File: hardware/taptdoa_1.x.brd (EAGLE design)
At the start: 64.8 x 63.2 mm, 67 parts, among them J1 105017-0001, U1 AP2112K-3.3TRG1, U2 STM32F103RBT6, Y1 8MHz

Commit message: v1.2 of board
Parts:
- removed TP21, TP22, TP4, TP5, TP6, TP7: TEST-POINT3X4, SparkFun-Connectors:PAD.03X.04
- moved J5 56.7 mm to (12.7, 58.4), turned to 0 degrees
- moved R6 46.6 mm to (15.2, 53.3)
- moved R1 46.2 mm to (53.3, 53.3)
- moved J3 44.0 mm to (35.6, 58.4), turned to 0 degrees
- moved R2 40.9 mm to (45.7, 53.3)
- moved R4 37.5 mm to (22.9, 53.3)
- moved R5 37.1 mm to (38.1, 53.3)
- moved R3 28.4 mm to (30.5, 53.3)
- moved TP3 21.0 mm to (36.1, 17.5)
- moved J2 19.4 mm to (16.5, 41.9), turned to 0 degrees
- moved TP2 17.0 mm to (35.9, 19.3)
- moved R15 16.5 mm to (55.6, 40.4)
- moved J1 15.2 mm to (63.2, 40.6)
- moved X1 7.73 mm to (5.08, 49.5)
- moved C1 6.84 mm to (15.2, 31.8)
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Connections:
- removed net PC0: R1.1, U2.8
- removed net PC1: R2.1, U2.9
- removed net PC2: R5.1, U2.10
- removed net PC3: R3.1, U2.11
- removed net PC4: R4.1, U2.24
- removed net PC5: R6.1, U2.25
- net OPAMP3_OUT: now also TP2.P$1; no longer TP21.P$1
- net PB2: now also TP3.P$1; no longer TP22.P$1
- net PB3: now also R1.1; no longer TP7.P$1
- net PB4: now also R2.1; no longer TP6.P$1
- net PB5: now also R5.1; no longer TP5.P$1
- net PB6: now also R3.1; no longer TP4.P$1
- net PB7: now also R4.1; no longer TP3.P$1
- net PB8: now also R6.1; no longer TP2.P$1
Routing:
- net +5V: track 60.5 -> 2.56 mm, vias 0 -> 1
- net PC3: track 32.6 -> 0.00 mm, vias 2 -> 0
- net PB8: track 2.27 -> 32.5 mm
- net PB3: track 4.86 -> 33.7 mm
- net PC4: track 28.6 -> 0.00 mm, vias 2 -> 0
- net PC5: track 27.9 -> 0.00 mm, vias 2 -> 0
- net PC0: track 27.7 -> 0.00 mm
- net PB4: track 2.13 -> 27.0 mm
- net PC1: track 23.0 -> 0.00 mm
- net PB7: track 4.89 -> 26.6 mm
- net PC2: track 21.0 -> 0.00 mm
- net PB6: track 3.42 -> 20.2 mm
- net USB_DP: track 40.4 -> 25.0 mm
- net PB5: track 6.32 -> 20.6 mm
- net NRST: track 34.3 -> 21.3 mm, vias 0 -> 2
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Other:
- board text added: "TapTDOA v1.2"
- board text removed: "TapTDOA v1.1"

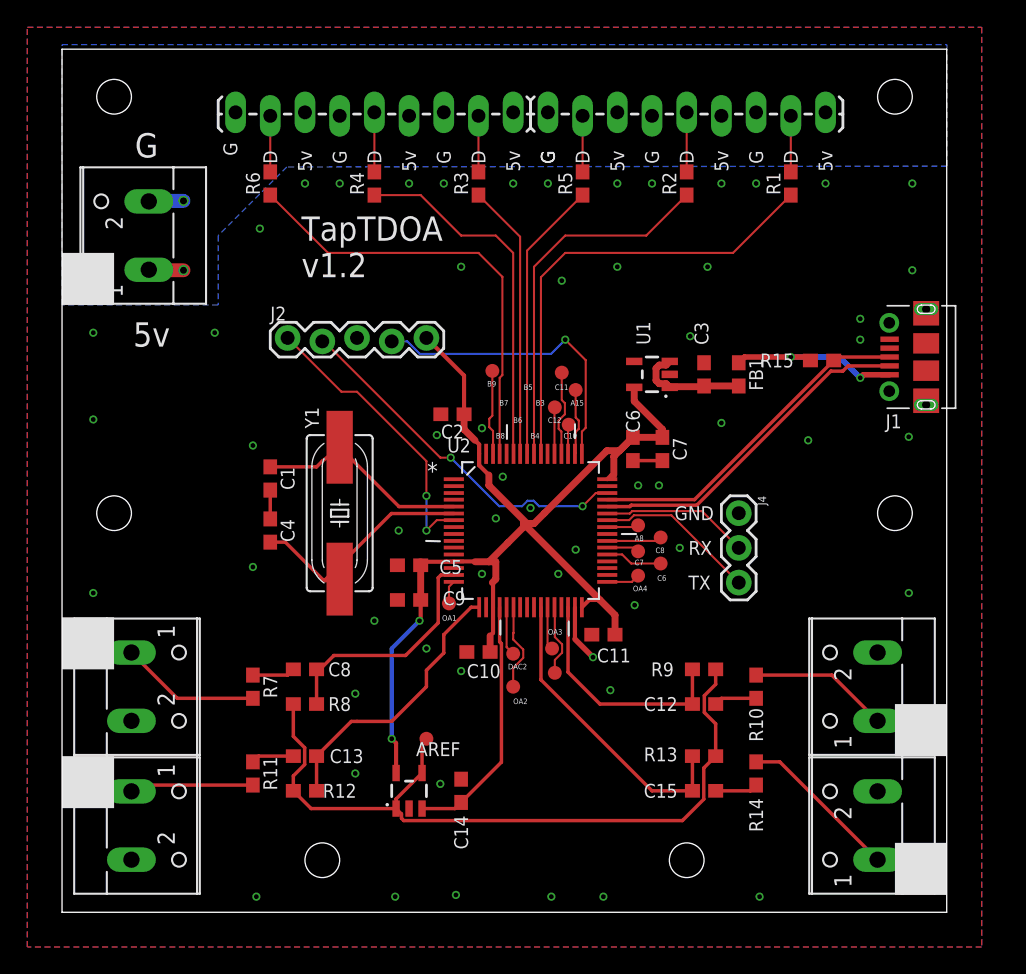
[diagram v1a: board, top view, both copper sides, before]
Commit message: working on LEDs, simple threshold detection for now, limited filtering
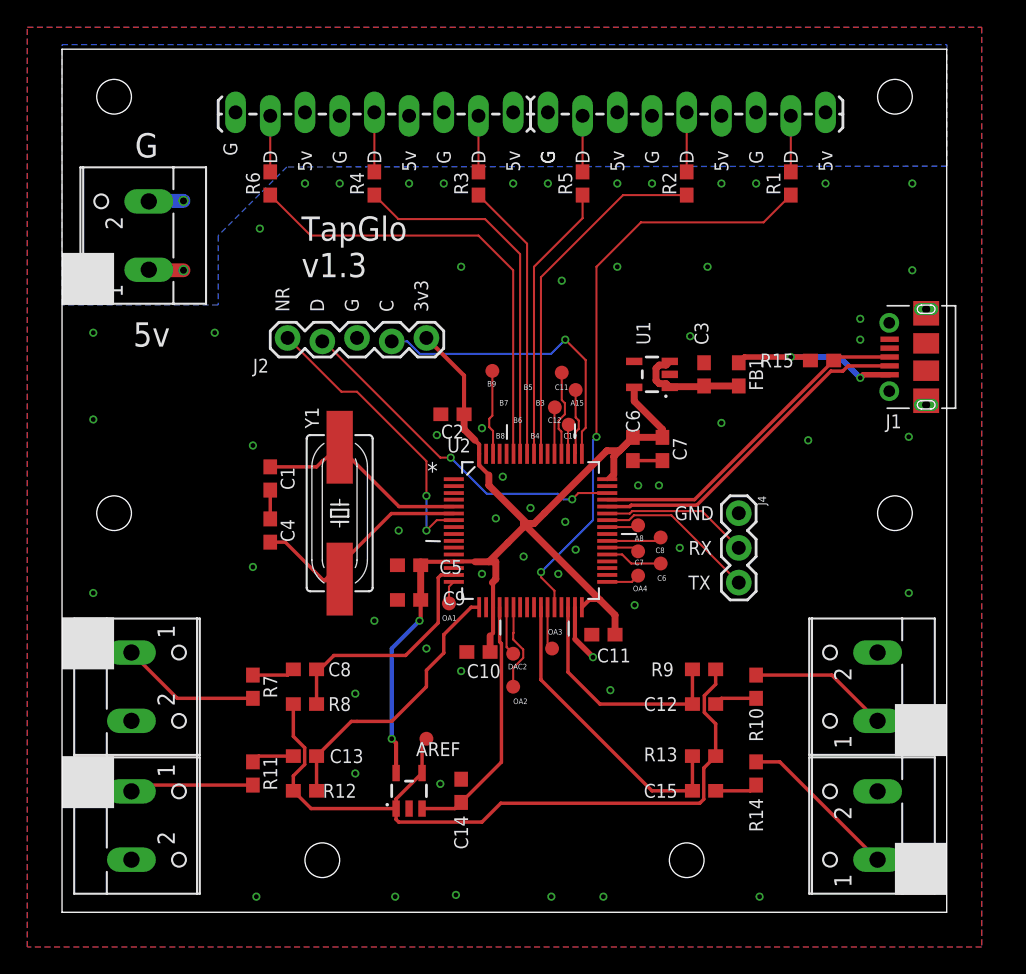
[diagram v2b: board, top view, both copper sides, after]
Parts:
- removed TP3: TEST-POINT3X4, SparkFun-Connectors:PAD.03X.04
- C12, C13, C15, C8: value 0.1uF -> 100pF
- R10, R11, R14, R7: value 10k -> 1k
- R12, R13, R8, R9: value 1k -> 100k
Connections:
- net PB2: now also R1.1; no longer TP3.P$1
- net PB3: now also R2.1; no longer R1.1
- net PB4: now also R5.1; no longer R2.1
- net PB5: now also R3.1; no longer R5.1
- net PB6: now also R4.1; no longer R3.1
- net PB7: now also R6.1; no longer R4.1
- net PB8: no longer R6.1
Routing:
- net PB2: track 5.25 -> 43.4 mm, vias 0 -> 2
- net PB8: track 32.5 -> 0.00 mm
- net PB3: track 33.7 -> 26.1 mm
- net PB7: track 26.6 -> 33.5 mm
- net PB6: track 20.2 -> 27.1 mm
- net PB4: track 27.0 -> 20.4 mm
- net PA13: track 26.6 -> 25.8 mm
- net GND: vias 59 -> 61
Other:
- board text added: "3v3"
- board text added: "C"
- board text added: "NR"
- board text added: "TapGlo v1.3"
- board text removed: "TapTDOA v1.2"

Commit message: re layout board
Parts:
- removed C14: 0.1uF, SparkFun-Capacitors:0603
- removed TP13, TP14, TP15, TP16, TP18, TP19, TP20: TEST-POINT3X4, SparkFun-Connectors:PAD.03X.04
- removed X1, X2, X3, X4, X5: (no value), con-wago-500:W237-102
- added C16: 0.1uF, SparkFun-Capacitors:0603
- added C17: 1.0uF, SparkFun-Capacitors:0603
- added C18, C19, C20, C21, C22, C23, C24, C25: 1nF, SparkFun-Capacitors:0603
- added C26, C27: 100uF, SparkFun-Capacitors:PANASONIC_D
- added FB2, FB3, FB4, FB5, FB6: 30Ω/1.8A, SparkFun-Coils:0603
- added J6, J7: (no value), SparkFun-Connectors:1X04_LOCK_LONGPADS
- added L1: 3.3µH/±20%/450mA, SparkFun-Coils:0805
- added R16, R17: 33, SparkFun-Resistors:0603
- added R18, R19: 75, SparkFun-Resistors:0603
- added TP3, TP4, TP5, TP6, TP7: TEST-POINT3X4, SparkFun-Connectors:PAD.03X.04
- added U$2: XT30XT30_THRUHOLE, XT30Male:ZT30
- added U4: SN74HCT245PWR, scanlime:TSSOP20
- C12, C13, C15, C8: value 100pF -> 1nF
- C3: value 1.0uF -> 4.7uF
- J3: device SparkFun-Connectors:1X09_LOCK_LONGPADS -> SparkFun-Connectors:1X18
- J5: device SparkFun-Connectors:1X09_LOCK_LONGPADS -> SparkFun-Connectors:1X06_LOCK
- R1, R2, R3, R4, R5, R6: value 100 -> 75
- R10, R11, R14, R7: value 1k -> 10k
- R12, R13, R8, R9: value 100k -> 10k
- moved TP10 35.4 mm to (13.6, 9.17)
- moved TP9 33.2 mm to (12.3, 16.9)
- moved J5 29.6 mm to (41.9, 53.3)
- moved TP11 29.2 mm to (48.3, 11.1)
- moved TP8 27.4 mm to (17.8, 16.5)
- moved R1 27.1 mm to (26.7, 48.3)
- moved J2 25.5 mm to (41.9, 39.4)
- moved TP1 24.9 mm to (36.3, 15.1)
- moved R6 24.7 mm to (39.4, 48.3)
- moved J3 24.1 mm to (11.4, 58.4)
- moved R2 17.3 mm to (29.2, 48.3)
- moved TP12 16.1 mm to (53.8, 17.1)
- moved R4 14.9 mm to (36.8, 48.3)
- moved FB1 14.5 mm to (63.5, 35.6), turned to 90 degrees
- moved C3 14.0 mm to (61.0, 39.4)
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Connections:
- removed net +5V: J3.3, J3.6, J3.9, J5.3, J5.6, J5.9, X1.1
- removed net DAC1_OUT2: TP19.P$1, U2.21
- removed net N$1: R7.2, X2.1
- removed net N$3: R11.2, X4.1
- removed net N$5: R14.2, X5.1
- removed net N$7: C12.2, R10.1
- removed net OPAMP1_IN: C13.1, R12.2, U2.17
- removed net OPAMP1_OUT: TP18.P$1, U2.16
- removed net OPAMP2_IN: C15.1, R13.2, U2.26
- removed net OPAMP2_OUT: TP20.P$1, U2.22
- removed net OPAMP3_IN: C8.1, R8.2, U2.15
- removed net OPAMP3_OUT: TP2.P$1, U2.27
- removed net OPAMP4_IN: C12.1, R9.2, U2.30
- removed net OPAMP4_OUT: TP14.P$1, U2.33
- removed net PA0-WKUP: U2.14
- removed net PA15: TP11.P$1, U2.50
- removed net PA7: U2.23
- removed net PA8: TP12.P$1, U2.41
- removed net PB10: U2.29
- removed net PB13: U2.34
- removed net PB14: U2.35
- removed net PB15: U2.36
- removed net PB2: R1.1, U2.28
- removed net PB3: R2.1, U2.55
- removed net PB4: R5.1, U2.56
- removed net PB5: R3.1, U2.57
- removed net PB6: R4.1, U2.58
- removed net PB7: R6.1, U2.59
- removed net PB8: U2.61
- removed net PB9: TP1.P$1, U2.62
- removed net PC10: TP10.P$1, U2.51
- removed net PC11: TP9.P$1, U2.52
- removed net PC12: TP8.P$1, U2.53
- removed net PC13-TAMPER-RTC: U2.2
- removed net PC14-OSC32_IN: U2.3
- removed net PC15-OSC32_OUT: U2.4
- removed net PC6: TP16.P$1, U2.37
- removed net PC7: TP13.P$1, U2.38
- removed net PC8: TP15.P$1, U2.39
- removed net PC9: U2.40
- removed net PD2: U2.54
- removed net VBAT: U2.1
- new net 5V: C26.+, C27.+, J3.1, J3.10, J3.13, J3.16, J3.4, J3.7, J5.1, J5.4, U$2.P$1, U4.1, U4.20
- new net HP1: C8.1, R7.2, R8.2, TP9.P$1
- new net HP2: C13.1, R11.2, R12.2, TP10.P$1
- new net HP3: C15.1, R13.2, R14.2, TP11.P$1
- new net HP4: C12.1, R10.2, R9.2, TP12.P$1
- new net N$10: R17.1, U2.45
- new net N$11: FB2.1, J1.5
- new net N$12: C17.1, L1.1, U1.5
- new net N$13: R1.1, U4.18
- new net N$14: R2.1, U4.17
- new net N$15: R5.1, U4.16
- new net N$16: R3.1, U4.15
- new net N$17: R4.1, U4.14
- new net N$18: R6.1, U4.13
- new net N$19: C8.2, FB3.1
- new net N$20: C15.2, FB5.1
- new net N$21: C13.2, FB4.1
- new net N$22: U2.53, U4.5
- new net N$23: C12.2, FB6.1
- new net N$24: U2.2, U4.4
- new net N$25: U2.3, U4.3
- new net N$26: U2.4, U4.2
- new net N$27: R18.1, U4.12
- new net N$28: R19.1, U4.11
- new net N$29: J5.2, R18.2
- new net N$30: J5.5, R19.2
- new net N$31: FB3.2, J6.1
- new net N$32: FB5.2, J7.1
- new net N$33: FB6.2, J7.3
- new net N$34: FB4.2, J6.3
- new net N$9: R16.1, U2.44
- new net OA1NEG: C22.1, U2.17
- new net OA1OUT: C22.2, TP4.P$1, U2.16
- new net OA2NEG: C23.1, U2.25
- new net OA2OUT: C23.2, TP3.P$1, U2.22
- new net OA3NEG: C24.1, U2.28
- new net OA3OUT: C24.2, TP1.P$1, U2.27
- new net OA4NEG: C25.2, U2.29
- new net OA4OUT: C25.1, TP2.P$1, U2.33
- new net SENSE1: C18.2, R7.1, TP8.P$1, U2.14, U2.15
- new net SENSE2: C19.2, R11.1, TP7.P$1, U2.23, U2.24
- new net SENSE3: C20.2, R14.1, TP6.P$1, U2.26, U2.34
- new net SENSE4: C21.2, R10.1, TP5.P$1, U2.30, U2.35
- net +3V3: now also L1.2; no longer U1.5
- net AREF: now also C18.1, C19.1, C20.1, C21.1
- net DAC1_OUT1: no longer C14.1
- net GND: now also C16.2, C17.2, C26.-, C27.-, FB2.2, J3.12, J3.15, J3.18, J3.3, J3.6, J3.9, J5.3, J5.6, J6.2, J6.4, J7.2, J7.4, U$2.P$2, U4.10, U4.19; no longer C14.2, J1.5, J3.1, J3.4, J3.7, J5.1, J5.4, J5.7, X1.2, X2.2, X3.2, X4.2, X5.2
- net LED0: now also J3.2; no longer J3.8
- net LED2: now also J3.8; no longer J3.2
- net LED3: now also J3.11; no longer J5.8
- net LED4: now also J3.14; no longer J5.5
- net LED5: now also J3.17; no longer J5.2
- net N$2: now also U2.39, U4.9; no longer C13.2, R11.1
- net N$4: now also U2.40, U4.8; no longer C15.2, R14.1
- net N$6: now also U2.51, U4.7; no longer R10.2, X3.1
- net N$8: now also U2.52, U4.6; no longer C8.2, R7.1
- net PA13: now also U2.50; no longer U2.46
- net USB_DM: now also R16.2; no longer U2.44
- net USB_DP: now also R17.2; no longer U2.45
- net VUSB2: now also C16.1
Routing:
- net PB2: track 43.4 -> 0.00 mm, vias 2 -> 0
- net AREF: track 55.8 -> 97.2 mm
- net PB7: track 33.5 -> 0.00 mm
- net SENSE3: track 0.00 -> 32.6 mm, vias 0 -> 2
- net 5V: track 0.00 -> 30.8 mm
- net PB6: track 27.1 -> 0.00 mm
- net SENSE4: track 0.00 -> 26.1 mm, vias 0 -> 2
- net PB3: track 26.1 -> 0.00 mm
- net SENSE2: track 0.00 -> 23.4 mm, vias 0 -> 2
- net SENSE1: track 0.00 -> 23.3 mm, vias 0 -> 2
- net OPAMP2_IN: track 22.3 -> 0.00 mm
- net OPAMP1_IN: track 20.4 -> 0.00 mm
- net PB4: track 20.4 -> 0.00 mm
- net PB5: track 20.4 -> 0.00 mm
- net OPAMP3_IN: track 17.5 -> 0.00 mm
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- added copper zone on layer 1, net 5V
- removed copper zone on layer 16, net +5V
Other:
- board size 64.8 x 63.2 mm -> 66 x 63.2 mm
- board text added: "-"
- board text added: "5V"
- board text added: "D0"
- board text added: "D1"
- board text added: "D2"
- board text added: "D3"
- board text added: "D4"
- board text added: "D5"
- board text added: "D6"
- board text added: "D7"
- board text added: "HP1"
- board text added: "HP2"
- board text added: "HP3"
- board text added: "HP4"
- board text added: "LP1"
- board text added: "LP2"
- board text added: "LP3"
- board text added: "LP4"
- board text added: "S1"
- board text added: "S2"
- board text added: "S3"
- board text added: "S4"
- board text removed: "5v"
- board text removed: "A15"
- board text removed: "A8"
- board text removed: "B3"
- board text removed: "B4"
- board text removed: "B5"
- board text removed: "B6"
- board text removed: "B8"
- board text removed: "C11"
- board text removed: "C6"
- board text removed: "C7"
- board text removed: "C8"
- board text removed: "DAC2"
- board text removed: "TapGlo v1.3"

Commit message: cleanup renumber
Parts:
- removed C27: 100uF, SparkFun-Capacitors:PANASONIC_D
- removed TP17: TEST-POINT3X4, SparkFun-Connectors:PAD.03X.04
- removed U4: SN74HCT245PWR, scanlime:TSSOP20
- added C14: 1nF, SparkFun-Capacitors:0603
- added TP13: TEST-POINT3X4, SparkFun-Connectors:PAD.03X.04
- added U3: STM32F103RBT6, ST Microelctronics_By_element14_Batch_1:QFP50P1200X1200X160-64N
- C1: value 22pF -> 100uF; device SparkFun-Capacitors:0603 -> SparkFun-Capacitors:PANASONIC_D
- C10: value 0.1uF -> 10nF
- C11: value 0.1uF -> 1.0uF
- C13, C19, C22: value 1nF -> 0.1uF
- C16: value 0.1uF -> 1nF
- C17: value 1.0uF -> 1nF
- C2: value 0.1uF -> 100uF; device SparkFun-Capacitors:0603 -> SparkFun-Capacitors:PANASONIC_D
- C26: value 100uF -> 1nF; device SparkFun-Capacitors:PANASONIC_D -> SparkFun-Capacitors:0603
- C3, C7: value 4.7uF -> 0.1uF
- C4: value 22pF -> 4.7uF
- C5: value 10nF -> 1.0uF
- C6: value 0.1uF -> 4.7uF
- C8: value 1nF -> 22pF
- C9: value 1.0uF -> 22pF
- J1: value 105017-0001 -> (none); device molex usb 105017-0001:MOLEX_105017-0001 -> SparkFun-Connectors:1X18
- J2: device SparkFun-Connectors:1X05_LOCK -> SparkFun-Connectors:1X06_LOCK
- J3: device SparkFun-Connectors:1X18 -> SparkFun-Connectors:1X05_LOCK
- J5: value (none) -> 105017-0001; device SparkFun-Connectors:1X06_LOCK -> molex usb 105017-0001:MOLEX_105017-0001
- R10, R9: value 10k -> 33
- R11: value 10k -> 4.7k
- R15: value 4.7k -> 10k
- R16, R17: value 33 -> 10k
- R18, R19: value 75 -> 10k
- R7, R8: value 10k -> 75
- U$1: value OPA344 -> XT30XT30_THRUHOLE; device SparkFun-IC-Amplifiers:SOT23-5 -> XT30Male:ZT30
- U$2: value XT30XT30_THRUHOLE -> OPA344; device XT30Male:ZT30 -> SparkFun-IC-Amplifiers:SOT23-5
- U1: value AP2112K-3.3TRG1 -> SN74HCT245PWR; device SparkFun-PowerIC:SOT23-5 -> scanlime:TSSOP20
- U2: value STM32F103RBT6 -> AP2112K-3.3TRG1; device ST Microelctronics_By_element14_Batch_1:QFP50P1200X1200X160-64N -> SparkFun-PowerIC:SOT23-5
- moved J1 61.2 mm to (11.4, 58.4), turned to 0 degrees
- moved R19 52.4 mm to (11.4, 7.62), turned to 0 degrees
- moved C16 49.0 mm to (21.6, 14.0)
- moved R8 48.5 mm to (44.5, 48.3), turned to 90 degrees
- moved U$1 46.7 mm to (0.00, 41.9)
- moved U$2 46.7 mm to (33.0, 8.89)
- moved C17 44.9 mm to (21.6, 8.89), turned to 90 degrees
- moved R11 44.9 mm to (58.4, 27.9)
- moved C26 43.6 mm to (54.6, 7.62), turned to 0 degrees
- moved C15 43.3 mm to (11.4, 10.2), turned to 180 degrees
- moved R7 41.9 mm to (41.9, 48.3), turned to 90 degrees
- moved R18 40.2 mm to (54.6, 10.2), turned to 180 degrees
- moved C13 38.1 mm to (43.3, 31.1), turned to 0 degrees
- moved R13 37.0 mm to (17.8, 14.0), turned to 270 degrees
- moved J3 35.9 mm to (41.9, 39.4)
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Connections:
- net +3V3: now also C13.1, C19.1, C22.1, C3.1, C4.1, J3.5, U$2.5, U3.13, U3.19, U3.32, U3.48, U3.64; no longer C2.1, C5.1, C6.1, C7.1, C9.1, J2.5, U$1.5, U2.13, U2.19, U2.32, U2.48, U2.64
- net 5V: now also C1.+, C2.+, J1.1, J1.10, J1.13, J1.16, J1.4, J1.7, J2.1, J2.4, U$1.P$1, U1.1, U1.20; no longer C26.+, C27.+, J3.1, J3.10, J3.13, J3.16, J3.4, J3.7, J5.1, J5.4, U$2.P$1, U4.1, U4.20
- net AREF: now also C16.1, C17.1, C23.1, C24.1, R17.1, R18.1, R19.1, TP8.P$1, U$2.1, U$2.4; no longer C18.1, C19.1, C20.1, C21.1, R13.1, R8.1, R9.1, TP17.P$1, U$1.1, U$1.4
- net DAC1_OUT1: now also U$2.3, U3.20; no longer U$1.3, U2.20
- net GND: now also C1.-, C13.2, C19.2, C2.-, C22.2, C4.2, C8.2, C9.1, FB1.2, J1.12, J1.15, J1.18, J1.3, J1.6, J1.9, J2.6, U$1.P$2, U$2.2, U1.10, U1.19, U2.2, U3.12, U3.18, U3.31, U3.47, U3.60, U3.63; no longer C1.2, C16.2, C17.2, C2.2, C26.-, C27.-, C4.1, C9.2, FB2.2, J3.12, J3.15, J3.18, J3.6, J3.9, J5.3, J5.6, U$1.2, U$2.P$2, U1.2, U2.12, U2.18, U2.31, U2.47, U2.60, U2.63, U4.10, U4.19
- net HP1: now also C14.1, R12.2, R13.2, TP2.P$1; no longer C8.1, R7.2, R8.2, TP9.P$1
- net HP2: now also C15.1, R14.2, R19.2, TP3.P$1; no longer C13.1, R11.2, R12.2, TP10.P$1
- net HP3: now also C26.1, R16.2, R18.2, TP12.P$1; no longer C15.1, R13.2, R14.2, TP11.P$1
- net HP4: now also C25.1, R15.2, R17.2, TP13.P$1; no longer C12.1, R10.2, R9.2, TP12.P$1
- net ID: now also J5.4; no longer J1.4
- net LED0: now also J1.2; no longer J3.2
- net LED1: now also J1.5; no longer J3.5
- net LED2: now also J1.8, R3.2; no longer J3.8, R5.2
- net LED3: now also J1.11, R4.2; no longer J3.11, R3.2
- net LED4: now also J1.14, R5.2; no longer J3.14, R4.2
- net LED5: now also J1.17; no longer J3.17
- net N$10: now also R9.1, U3.45; no longer R17.1, U2.45
- net N$11: now also FB1.1, J5.5; no longer FB2.1, J1.5
- net N$12: now also C5.1, U2.5; no longer C17.1, U1.5
- net N$13: now also U1.18; no longer U4.18
- net N$14: now also U1.17; no longer U4.17
- net N$15: now also R3.1, U1.16; no longer R5.1, U4.16
- net N$16: now also R4.1, U1.15; no longer R3.1, U4.15
- net N$17: now also R5.1, U1.14; no longer R4.1, U4.14
- net N$18: now also U1.13; no longer U4.13
- net N$19: now also C14.2; no longer C8.2
- net N$2: now also U1.9, U3.39; no longer U2.39, U4.9
- net N$20: now also C26.2, FB6.1; no longer C15.2, FB5.1
- net N$21: now also C15.2; no longer C13.2
- net N$22: now also U1.5, U3.53; no longer U2.53, U4.5
- net N$23: now also C25.2, FB5.1; no longer C12.2, FB6.1
- net N$24: now also U1.4, U3.2; no longer U2.2, U4.4
- net N$25: now also U1.3, U3.3; no longer U2.3, U4.3
- net N$26: now also U1.2, U3.4; no longer U2.4, U4.2
- net N$27: now also R7.1, U1.12; no longer R18.1, U4.12
- net N$28: now also R8.1, U1.11; no longer R19.1, U4.11
- net N$29: now also J2.2, R7.2; no longer J5.2, R18.2
- net N$30: now also J2.5, R8.2; no longer J5.5, R19.2
- net N$32: now also FB6.2; no longer FB5.2
- net N$33: now also FB5.2; no longer FB6.2
- net N$4: now also U1.8, U3.40; no longer U2.40, U4.8
- net N$6: now also U1.7, U3.51; no longer U2.51, U4.7
- net N$8: now also U1.6, U3.52; no longer U2.52, U4.6
- net N$9: now also R10.1, U3.44; no longer R16.1, U2.44
- net NRST: now also J3.1, U3.7; no longer J2.1, U2.7
- net OA1NEG: now also C18.1, U3.17; no longer C22.1, U2.17
- net OA1OUT: now also C18.2, TP6.P$1, U3.16; no longer C22.2, TP4.P$1, U2.16
- net OA2NEG: now also C20.1, U3.25; no longer C23.1, U2.25
- net OA2OUT: now also C20.2, TP7.P$1, U3.22; no longer C23.2, TP3.P$1, U2.22
- net OA3NEG: now also C21.1, U3.28; no longer C24.1, U2.28
- net OA3OUT: now also C21.2, TP9.P$1, U3.27; no longer C24.2, TP1.P$1, U2.27
- net OA4NEG: now also C12.2, U3.29; no longer C25.2, U2.29
- net OA4OUT: now also C12.1, TP1.P$1, U3.33; no longer C25.1, TP2.P$1, U2.33
- net PA13: now also J3.2, U3.50; no longer J2.2, U2.50
- net PA14: now also J3.4, U3.49; no longer J2.4, U2.49
- net PD0_OSC_IN: now also C8.1, U3.5; no longer C1.1, U2.5
- net PD1_OSC_OUT: now also C9.2, U3.6; no longer C4.2, U2.6
- net SENSE1: now also C16.2, R13.1, TP4.P$1, U3.14, U3.15; no longer C18.2, R7.1, TP8.P$1, U2.14, U2.15
- net SENSE2: now also C17.2, R14.1, TP5.P$1, U3.23, U3.24; no longer C19.2, R11.1, TP7.P$1, U2.23, U2.24
- net SENSE3: now also C24.2, R16.1, TP10.P$1, U3.26, U3.34; no longer C20.2, R14.1, TP6.P$1, U2.26, U2.34
- net SENSE4: now also C23.2, R15.1, TP11.P$1, U3.30, U3.35; no longer C21.2, R10.1, TP5.P$1, U2.30, U2.35
- net UART1_RX: now also U3.43; no longer U2.43
- net UART1_TX: now also U3.42; no longer U2.42
- net USB_DM: now also J5.2, R10.2; no longer J1.2, R16.2
- net USB_DP: now also J5.3, R11.1, R9.2; no longer J1.3, R15.1, R17.2
- net VUSB: now also FB2.1, J5.1, R11.2; no longer FB1.1, J1.1, R15.2
- net VUSB2: now also C6.1, C7.1, FB2.2, U2.1, U2.3; no longer C16.1, C3.1, FB1.2, U1.1, U1.3
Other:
- board text removed: "C10"
- board text removed: "C12"
